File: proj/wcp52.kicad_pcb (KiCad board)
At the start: 4 copper layers, 100 x 100 mm, 279 parts, among them J1 MicroUSB-B, Q1 MMBT3906, Q10 MMBT3904, Q11 BFR540, Q12 BFR540, Q13 MMBT3904, Q14 MMBT3904, Q15 MMBT3904, Q16 MMBT3904, Q17 PZT2907A, Q18 PZT2907A, Q19 MMBT3904, Q2 IRLML6402, Q3 AOD417, Q4 MMBT3906, Q5 2N7002, Q6 2N7002, Q7 MMBT3906, Q8 2N7002, Q9 2N7002, U1 TL431AIDBZ, U10 MASWSS0162, U11 AD8310ARMZ, U12 PIC24FJ128GA306-I/PT, U13 FT230XS, U14 L78M05CDT, U15 MC79M05CDT, U16 AZ1117CH-1.8TRG1, U17 MCP1700T-vv02E/TT, U2 LM393M, U3 LMH6714MF, U4 AD9958BCPZ, U5 LMH6714MF, U6 AD8000YRDZ, U7 THS3001IDGN, U8 MAADSS0008, U9 MASWSS0162, X1 25 MHz

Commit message: Begin swapping MCU
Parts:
- moved U4 37.9 mm to (40.8, 149.2)
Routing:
- net /Comm/IN_USBD_P: track 5.43 -> 0.00 mm
- net /Comm/IN_USBD_N: track 5.88 -> 0.53 mm

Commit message: PCB work, mostly mechanical
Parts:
- added C114, C120: 10u, IPC7351-Nominal:CAPC2012X70, F.Cu at (125.0, 135.1)
- added C115, C116, C117, C118, C119, C121, C122, C123, C124: 100n, IPC7351-Nominal:CAPC1608X55, F.Cu at (125.0, 135.1)
- added C125: 1u, IPC7351-Nominal:CAPC2012X70, F.Cu at (125.0, 135.1)
- added C126, C127: 15p, IPC7351-Nominal:CAPC1005X55, F.Cu at (125.0, 135.1)
- added J2: IN1, manuf:CONN-BNC-1-1337543-0, F.Cu at (97.0, 112.0)
- added J3: IN2, manuf:CONN-BNC-1-1337543-0, F.Cu at (125.0, 112.0)
- added J4: OUT, manuf:CONN-BNC-1-1337543-0, F.Cu at (153.0, 112.0)
- added MP2: SCREW, mech:SCREW-3-SUPPORTED, F.Cu at (85.0, 35.0)
- added MP3: SCREW, mech:SCREW-3-SUPPORTED, F.Cu at (165.0, 35.0)
- added MP4: SCREW, mech:SCREW-3-SUPPORTED, F.Cu at (165.0, 115.0)
- added MP5: SCREW, mech:SCREW-3-SUPPORTED, F.Cu at (85.0, 115.0)
- added X2: 12MHz, IPC7351-Nominal:XTAL1200X480X460, F.Cu at (125.0, 135.1)
- U12: value PIC24FJ128GA306-I/PT -> ATSAM4S16CA-AU; footprint IPC7351-Nominal:QFP50P1200X1200X120-64 -> IPC7351-Nominal:QFP50P1600X1600X160-100
- moved U12 197.2 mm to (202.0, 61.0)
- moved U4 151.4 mm to (189.2, 119.7), turned to 90 degrees
- moved Q3 120.1 mm to (97.5, 35.8)
- moved C1 120.1 mm to (103.5, 29.5)
- moved C2 120.1 mm to (109.0, 39.0)
- moved C3 120.1 mm to (91.5, 39.5)
- moved D1 120.1 mm to (109.5, 35.1)
- moved D2 120.1 mm to (109.5, 43.0)
- moved DS1 120.1 mm to (95.5, 45.5)
- moved Q1 120.1 mm to (94.0, 43.0)
- moved Q14 120.1 mm to (103.8, 44.8)
- moved Q2 120.1 mm to (91.5, 36.0)
- moved R1 120.1 mm to (91.5, 31.0)
- moved R10 120.1 mm to (90.5, 43.5)
- moved R11 120.1 mm to (91.0, 41.5)
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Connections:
- net Net-(U12-Pad44) renamed /MPU/TX
- net Net-(U12-Pad46) renamed /MPU/RX
- net Net-(U12-Pad51) renamed /MPU/TDI
- U12 pad 1: Net-(U12-Pad1) -> /MPU/ADC_VREF
- U12 pad 11: Net-(U12-Pad11) -> /MPU/VCORE
- U12 pad 16: Net-(U12-Pad16) -> /MPU/VCORE
- U12 pad 2: Net-(U12-Pad2) -> GND
- U12 pad 20: GND -> Net-(U12-Pad20)
- U12 pad 25: GND -> Net-(U12-Pad25)
- U12 pad 26: +3.3 -> GND
- U12 pad 27: Net-(U12-Pad27) -> +3.3
- U12 pad 36: Net-(U12-Pad36) -> /MPU/VCORE
- U12 pad 38: +3.3 -> Net-(U12-Pad38)
- U12 pad 41: GND -> Net-(U12-Pad41)
- U12 pad 45: Net-(U12-Pad45) -> GND
- U12 pad 50: Net-(U12-Pad50) -> +3.3
- U12 pad 56: Net-(U12-Pad56) -> /MPU/VCORE
- U12 pad 9: GND -> Net-(U12-Pad9)
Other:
- net class Default: clearance 0.254 -> 0.2; trace_width 0.254 -> 0.2; via_dia 0.889 -> 0.8; via_drill 0.635 -> 0.4
- rule trace_clearance: 0.254 -> 0.2
- rule trace_min: 0.254 -> 0.15
- rule via_min_drill: 0.508 -> 0.3
- rule via_min_size: 0.889 -> 0.6

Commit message: Layout most analog bits
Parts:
- added J5: CONN-PJ-037A, conn-cui:CONN-PJ-037A, F.Cu at (100.0, 119.0)
- added MP1: SHIELD, manuf:LAIRD-BMI-S-203, F.Cu at (134.0, 100.0)
- C30, C31, C32, C33, C34, C35, C36, C37, C38, C39, C40, C41, C71, C72, R13, R15, R17, R18: moved to B.Cu
- J2, J3, J4: footprint manuf:CONN-BNC-1-1337543-0 -> manuf:CONN-TE-1814400
- moved U12 146.3 mm to (62.8, 105.8)
- moved R85 133.4 mm to (158.0, 35.0)
- moved L6 128.5 mm to (150.0, 33.0), turned to 180 degrees
- moved C102 123.2 mm to (163.0, 41.0), turned to 270 degrees
- moved DZ9 121.7 mm to (166.0, 41.1)
- moved C100 121.3 mm to (158.0, 41.0), turned to 270 degrees
- moved L7 120.7 mm to (121.0, 33.5), turned to 180 degrees
- moved Q19 116.8 mm to (129.0, 31.0), turned to 90 degrees
- moved C110 115.8 mm to (135.0, 30.0), turned to 180 degrees
- moved R95 113.0 mm to (129.0, 35.0), turned to 180 degrees
- moved D3 112.9 mm to (153.0, 43.0), turned to 270 degrees
- moved R94 111.6 mm to (111.0, 45.5), turned to 270 degrees
- moved R93 110.8 mm to (112.5, 45.5), turned to 90 degrees
- moved U16 110.3 mm to (137.5, 35.0)
- moved Q18 110.2 mm to (118.1, 43.0)
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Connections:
- U8 pad 2: Net-(U8-Pad2) -> GND
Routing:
- net /Synth/CH1_P: track 0.00 -> 44.3 mm, vias 0 -> 1
- net /Synth/CH1_N: track 0.00 -> 44.2 mm, vias 0 -> 1
- net /Synth/CH0_N: track 0.00 -> 16.7 mm, vias 0 -> 1
- net /Synth/CH0_P: track 0.00 -> 16.7 mm, vias 0 -> 1

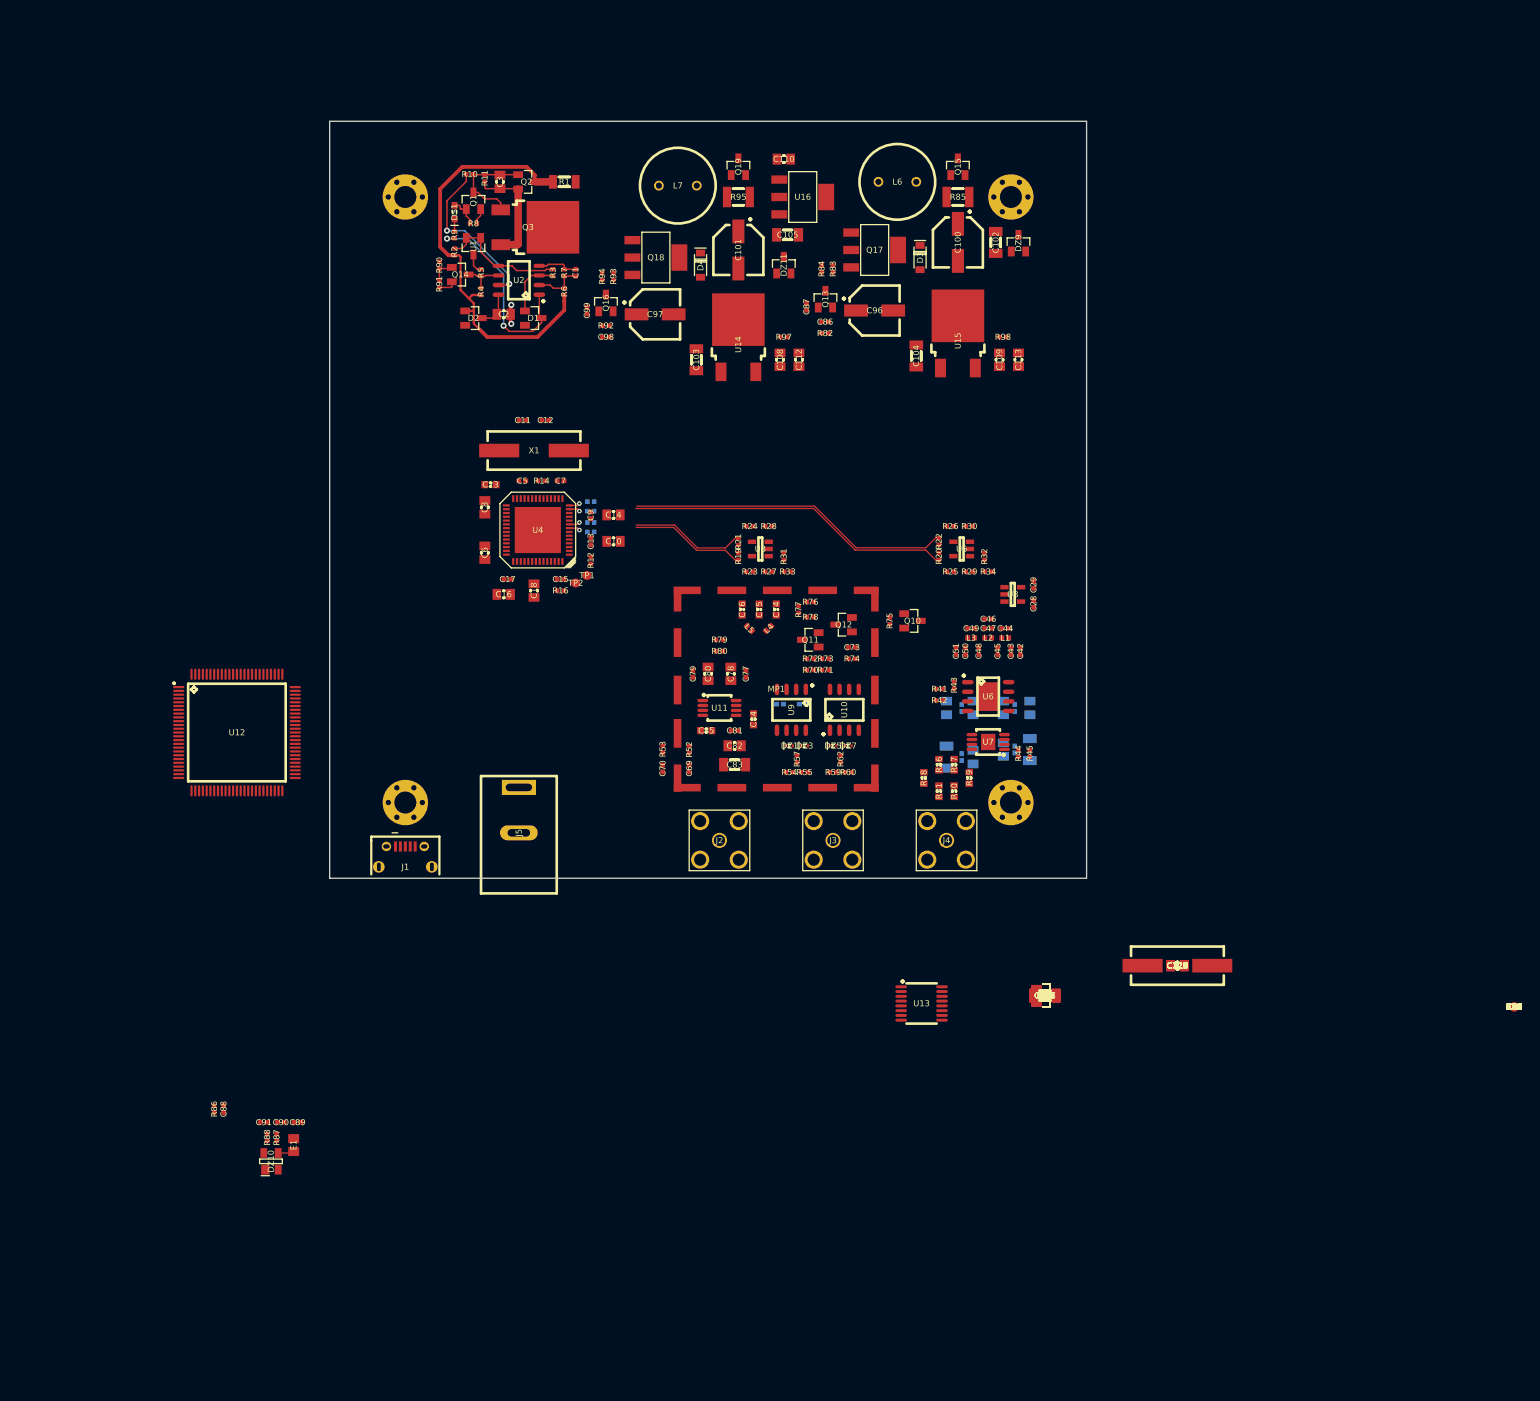
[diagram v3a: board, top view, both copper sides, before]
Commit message: Add side bars, ground plane
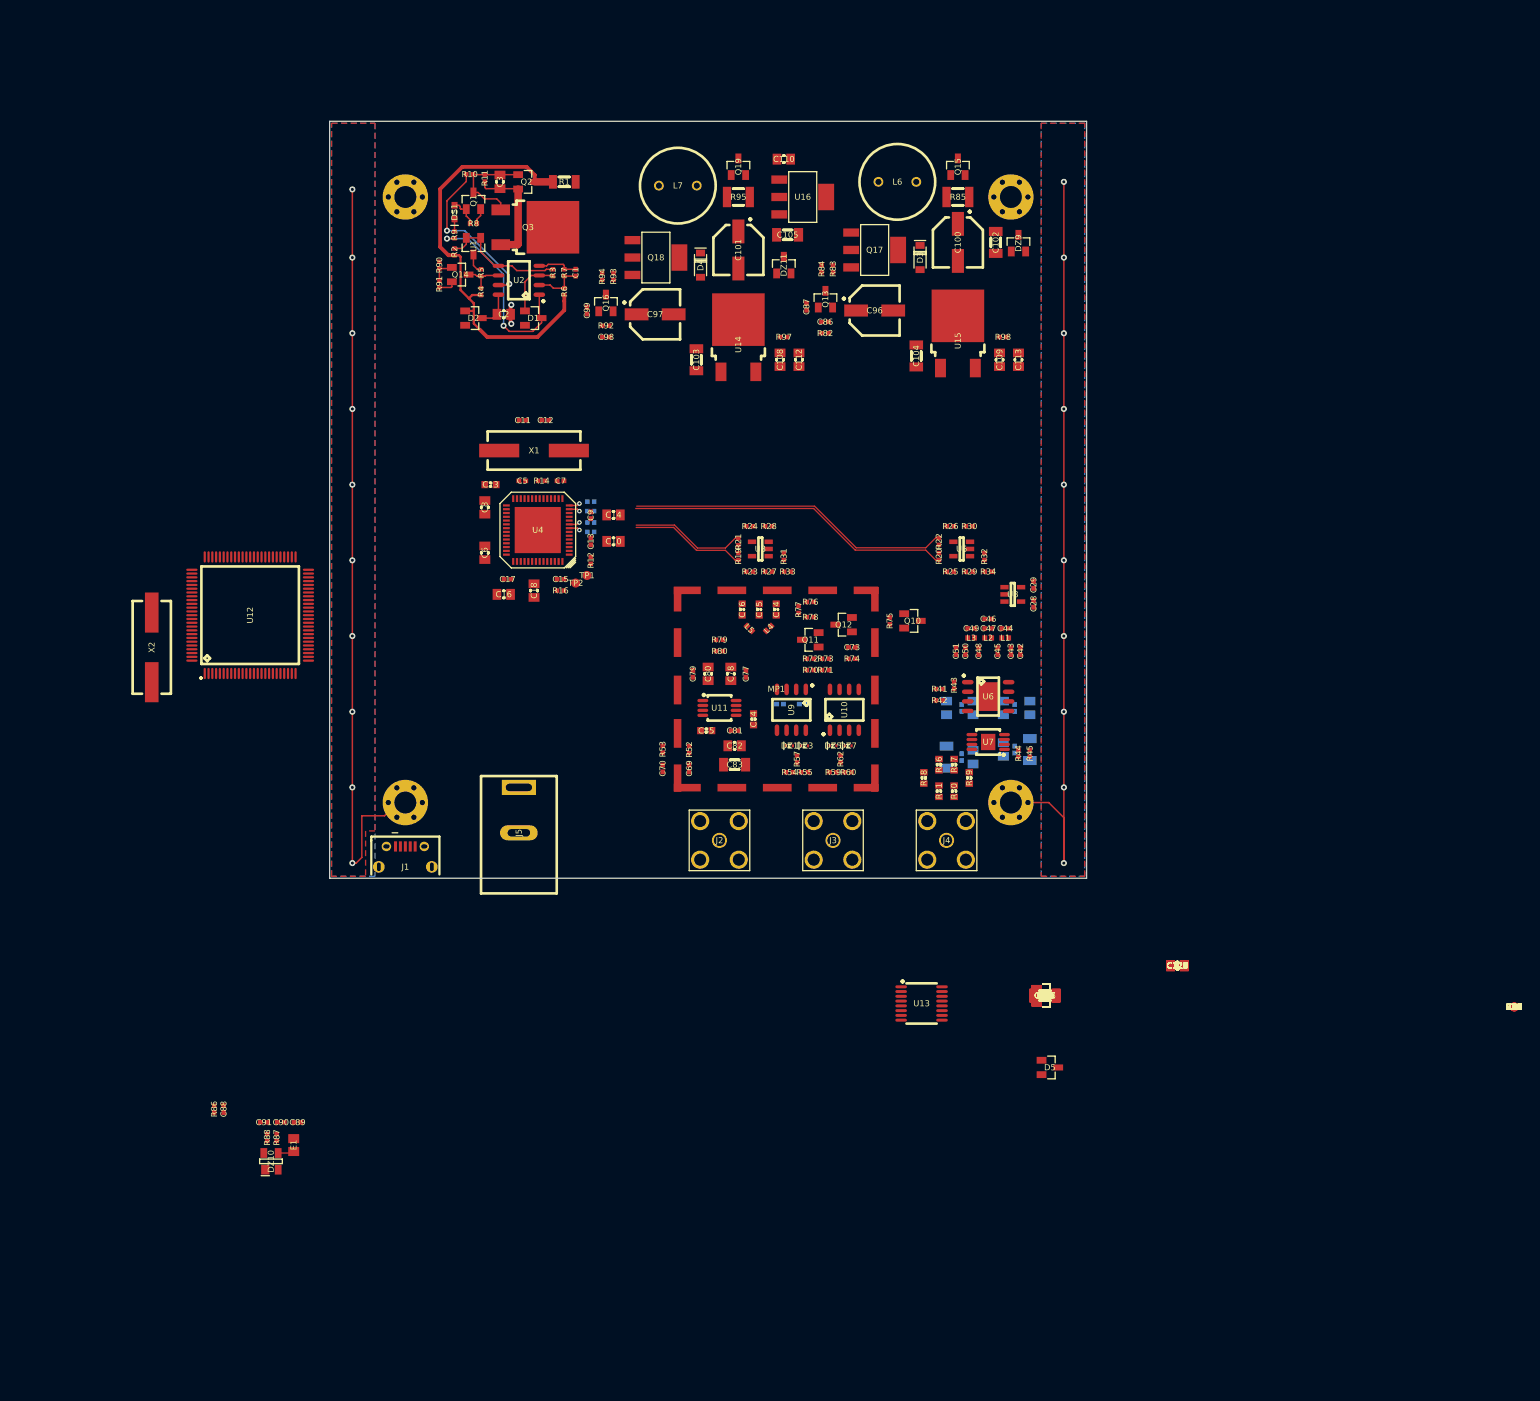
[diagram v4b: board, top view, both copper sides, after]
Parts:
- moved X2 141.9 mm to (51.5, 94.5), turned to 90 degrees
- moved U12 15.6 mm to (64.5, 90.2), turned to 90 degrees
- moved D5 9.52 mm to (170.2, 150.0)
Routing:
- net GND: track 13.0 -> 217.1 mm, vias 2 -> 22
- added copper zone on B.Cu, net GND
- added copper zone on F.Cu, net GND
- added copper zone on In2.Cu, net GND

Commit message: Lots of routing
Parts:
- moved R81 111.0 mm to (125.2, 110.0), turned to 270 degrees
- moved R14 5.52 mm to (108.5, 72.0)
- moved C7 3.16 mm to (108.5, 73.5), turned to 0 degrees
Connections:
- net Net-(L6-Pad1) renamed /DCDC/ISEN_N9
- net Net-(L7-Pad1) renamed /DCDC/ISEN_3V3
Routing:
- net /DCDC/IN: track 0.00 -> 99.4 mm, vias 0 -> 11
- net /DCDC/FDBK_3V3: track 0.00 -> 52.8 mm, vias 0 -> 4
- net /DCDC/FDBK_N9: track 0.00 -> 52.3 mm, vias 0 -> 4
- net GND: track 217.1 -> 256.7 mm, vias 22 -> 23
- net -9: track 0.00 -> 34.8 mm
- net /DCDC/SW_3V3: track 0.00 -> 29.9 mm, vias 0 -> 3
- net /DCDC/SW_N9: track 0.00 -> 29.9 mm, vias 0 -> 3
- net /OutputAmp/LPF/B: track 0.00 -> 21.9 mm
- net /InputFrontend/IN1: track 0.00 -> 19.3 mm
- net /InputFrontend/Buffer_Filter/IN: track 0.00 -> 17.6 mm
- net Net-(C12-Pad1): track 0.00 -> 16.7 mm
- net +3.3: track 0.00 -> 16.4 mm
- net Net-(C11-Pad1): track 0.00 -> 16.1 mm
- net Net-(C73-Pad1): track 0.00 -> 15.2 mm
- net Net-(R44-Pad1): track 0.00 -> 15.2 mm
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
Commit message: Lots of layout work
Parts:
- added E3: 1k@100, IPC7351-Nominal:INDC1608X95, F.Cu at (96.5, 88.0)
- added J6: JLINK, conn-100mil:CONN-100MIL-M-2x10-SHROUD, F.Cu at (107.0, 55.0)
- added R100, R101, R102, R99: 4k7, IPC7351-Nominal:RESC1005X40, F.Cu at (125.0, 135.1)
- added TP5: 3V3MCU, conn-test:TEST-SMD-SMALL, F.Cu at (87.0, 75.2)
- R13, R15, R17, R18: moved to F.Cu
- U13: value FT230XS -> FT230XS_DNP
- moved C4 178.3 mm to (90.0, 33.5), turned to 90 degrees
- moved R89 152.0 mm to (83.5, 107.5), turned to 180 degrees
- moved D5 117.5 mm to (86.0, 68.0), turned to 270 degrees
- moved C117 114.0 mm to (90.8, 75.5), turned to 180 degrees
- moved C126 113.0 mm to (89.8, 79.0), turned to 270 degrees
- moved C121 110.9 mm to (90.8, 81.5), turned to 180 degrees
- moved C106 110.4 mm to (82.9, 72.0), turned to 270 degrees
- moved C116 109.9 mm to (90.8, 83.5), turned to 180 degrees
- moved C127 109.6 mm to (89.8, 86.0), turned to 270 degrees
- moved U17 108.0 mm to (86.0, 72.0), turned to 90 degrees
- moved C118 107.6 mm to (105.5, 66.2), turned to 90 degrees
- moved C111 105.7 mm to (89.0, 72.0), turned to 90 degrees
- moved C125 104.9 mm to (93.5, 89.0), turned to 270 degrees
- moved C114 99.6 mm to (99.5, 89.0), turned to 270 degrees
- moved C120 97.4 mm to (102.0, 89.0), turned to 270 degrees
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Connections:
- C114 pad 1: +3.3 -> +3.3SB
- C121 pad 1: +3.3 -> +3.3SB
- C122 pad 1: +3.3 -> +3.3SB
- C123 pad 1: +3.3 -> +3.3SB
- C124 pad 1: +3.3 -> +3.3SB
- C90 pad 1: /Comm/USBD_N -> /Comm/OUT_USBD_N
- C91 pad 1: /Comm/USBD_P -> /Comm/OUT_USBD_P
- DZ10 pad 2: /Comm/IN_USBD_N -> /Comm/USBD_N
- DZ10 pad 4: /Comm/IN_USBD_P -> /Comm/USBD_P
- J1 pad 2: /Comm/USBD_N -> /Comm/OUT_USBD_N
- J1 pad 3: /Comm/USBD_P -> /Comm/OUT_USBD_P
- R87 pad 1: /Comm/IN_USBD_N -> /Comm/USBD_N
- R87 pad 2: /Comm/USBD_N -> /Comm/OUT_USBD_N
- R88 pad 1: /Comm/IN_USBD_P -> /Comm/USBD_P
- R88 pad 2: /Comm/USBD_P -> /Comm/OUT_USBD_P
- U12 pad 10: +3.3 -> +3.3SB
- U12 pad 27: +3.3 -> +3.3SB
- U12 pad 44: /MPU/TX -> /MPU/SER_FROM_MPU
- U12 pad 46: /MPU/RX -> /Comm/SER_FROMUSB
- U12 pad 50: +3.3 -> +3.3SB
- U12 pad 60: Net-(U12-Pad60) -> /MPU/#RST
- U12 pad 69: +3.3 -> +3.3SB
- U12 pad 88: /MPU/USBD_N -> /Comm/USBD_N
- U12 pad 89: /MPU/USBD_P -> /Comm/USBD_P
- U12 pad 91: +3.3 -> +3.3SB
- U12 pad 98: +3.3 -> +3.3SB
- U13 pad 4: /Comm/SER_TOUSB -> /MPU/SER_FROM_MPU
- U13 pad 8: /Comm/IN_USBD_P -> /Comm/USBD_P
- U13 pad 9: /Comm/IN_USBD_N -> /Comm/USBD_N
- U2 pad 1: Net-(D1-Pad3) -> Net-(R10-Pad2)
- U2 pad 2: Net-(C1-Pad2) -> Net-(Q14-Pad3)
- U2 pad 3: Net-(D1-Pad1) -> Net-(R2-Pad2)
- U2 pad 5: Net-(R2-Pad2) -> Net-(D1-Pad1)
- U2 pad 6: Net-(Q14-Pad3) -> Net-(C1-Pad2)
- U2 pad 7: Net-(R10-Pad2) -> Net-(D1-Pad3)
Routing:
- net /Comm/USBPWR: track 2.13 -> 69.0 mm, vias 0 -> 4
- net /DCDC/IN: track 99.4 -> 35.6 mm, vias 11 -> 0
- net /Comm/USBD_N: track 0.00 -> 62.1 mm
- net /Comm/USBD_P: track 0.00 -> 61.4 mm
- net Net-(D2-Pad1): track 57.1 -> 9.31 mm
- net GND: track 256.7 -> 298.3 mm, vias 23 -> 53
- net /MPU/TCK: track 0.00 -> 39.7 mm
- net /MPU/TDI: track 0.00 -> 36.7 mm
- net /MPU/TDO: track 0.00 -> 31.5 mm
- net /MPU/TMS: track 0.00 -> 26.4 mm
- net /Synth/CH1_N: track 46.5 -> 20.6 mm, vias 1 -> 2
- net /Synth/CH1_P: track 46.6 -> 21.1 mm, vias 1 -> 2
- net /DCDC/FDBK_N9: track 52.3 -> 27.0 mm, vias 4 -> 2
- net /DCDC/FDBK_3V3: track 52.8 -> 29.0 mm
- net /MPU/#RST: track 0.00 -> 22.2 mm
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
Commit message: Some PCB work
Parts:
- DZ2, DZ4, DZ6, DZ8, R56, R58, R61, R63, R66, R67: moved to B.Cu
- moved R56 102.5 mm to (134.0, 110.2), turned to 90 degrees
- moved R58 98.3 mm to (139.5, 107.2), turned to 90 degrees
- moved R35 98.0 mm to (165.2, 69.8)
- moved R36 97.6 mm to (162.5, 73.0), turned to 270 degrees
- moved R61 97.1 mm to (139.8, 110.2), turned to 90 degrees
- moved R37 94.9 mm to (164.2, 75.0), turned to 180 degrees
- moved R40 93.4 mm to (166.5, 75.0)
- moved R63 93.0 mm to (145.2, 107.2), turned to 90 degrees
- moved R66 92.3 mm to (147.2, 104.2), turned to 180 degrees
- moved R67 91.8 mm to (147.2, 105.5), turned to 180 degrees
- moved R69 90.8 mm to (150.0, 102.0), turned to 180 degrees
- moved R38 88.1 mm to (165.2, 84.0), turned to 90 degrees
- moved R65 87.4 mm to (150.0, 110.5), turned to 180 degrees
- moved R68 86.9 mm to (150.0, 111.8)
- moved R39 86.9 mm to (166.8, 84.0), turned to 90 degrees
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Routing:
- net -5: track 4.36 -> 24.3 mm, vias 0 -> 2
- net Net-(C72-Pad1): track 0.00 -> 18.1 mm, vias 0 -> 3
- net Net-(C71-Pad1): track 0.00 -> 15.1 mm, vias 0 -> 3
- net Net-(Q8-Pad3): track 0.00 -> 11.4 mm, vias 0 -> 1
- net Net-(Q4-Pad3): track 0.00 -> 11.1 mm
- net Net-(Q5-Pad3): track 0.00 -> 10.6 mm
- net Net-(DZ7-Pad2): track 0.00 -> 9.86 mm, vias 0 -> 4
- net Net-(DZ3-Pad2): track 0.00 -> 9.79 mm, vias 0 -> 2
- net Net-(Q6-Pad3): track 0.00 -> 9.59 mm
- net GND: track 298.3 -> 306.3 mm, vias 53 -> 59
- net Net-(C28-Pad1): track 0.00 -> 7.09 mm
- net Net-(DZ5-Pad1): track 0.00 -> 5.46 mm, vias 0 -> 2
- net Net-(DZ1-Pad1): track 0.00 -> 5.46 mm, vias 0 -> 2
- net /OutputAmp/INPUT: track 0.00 -> 5.25 mm
- net Net-(Q9-Pad3): track 0.00 -> 4.88 mm, vias 0 -> 1
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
